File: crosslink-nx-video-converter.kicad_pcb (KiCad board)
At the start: 6 copper layers, 105.8 x 68 mm, 282 parts, among them J1 DC_SOCKET, J2 031-70526-21, J3 031-70526-21, J4 WE_68715014522_ONE-SIDE, J5 FTSH-105-01-F-DV-K, J6 WE_68715014522_ONE-SIDE, J7 2X05, J8 61300411121, Q1 2N7002, Q2 AO3401A, Q3 AO3401A, Q4 2N7002, Q5 AO3401A, Q6 2N7002, SW1 SW_DIP_x06, U1 MP20073, U10 AP7330-W5-7, U11 LIFCL-40-9BG256C, U12 MT41K128M16JT-125_K, U15 GS2971A, U16 GS2988, U17 SC18IS602BIPW, U18 W25Q32JVSSIQ, U2 LM339, U3 LM339, U5 AP62301WU-7, U6 AP62301WU-7, U7 AP62301WU-7, U8 AP7330-W5-7, U9 AP7330-W5-7, Y1 ABM7_27.000MH_D2Y_T, Y2 OSC40M-3.3_S5

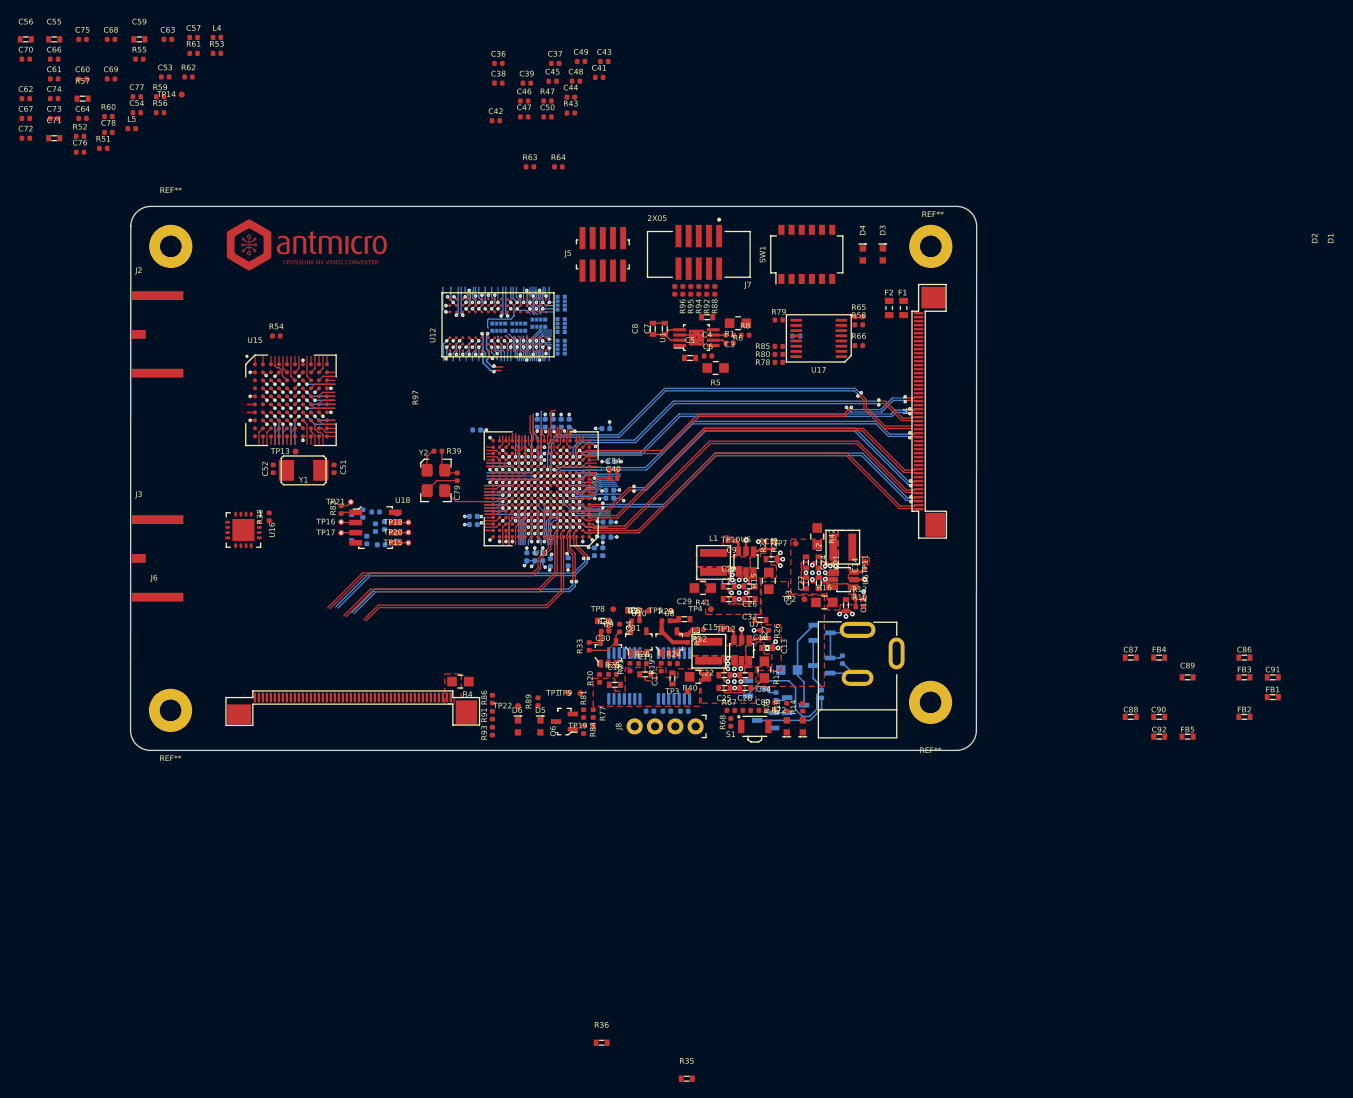
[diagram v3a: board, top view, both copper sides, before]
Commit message: Finished component placement
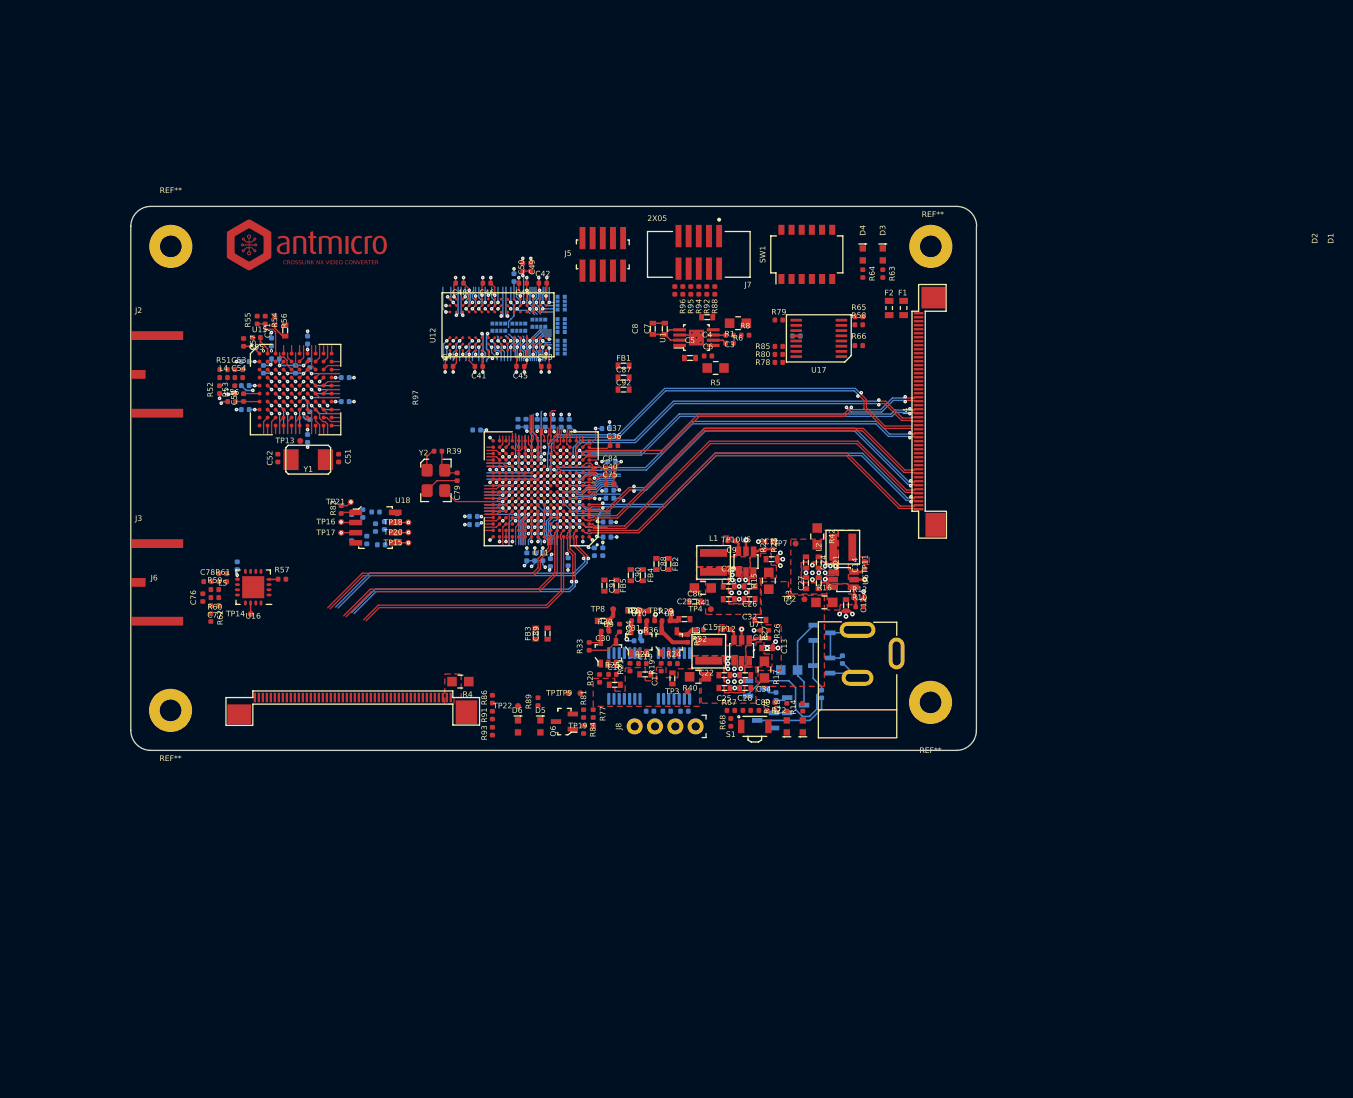
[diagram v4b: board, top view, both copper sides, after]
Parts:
- C38, C39, C60, C61, C62, C63, C64, C66, C67, C68, C69, C70, C72, C73, C74, R38, R47: moved to B.Cu
- C55: value C_47n_0603 -> C_47n_0402; footprint crosslink-nx-video-converter-footprints:0603-cap -> antmicro-footprints:0402-cap
- C56, C59: value C_470n_0603 -> C_470n_0402; footprint crosslink-nx-video-converter-footprints:0603-cap -> antmicro-footprints:0402-cap
- R35: value R_18k7_1%_0603 -> R_18k7_0402; footprint crosslink-nx-video-converter-footprints:0603-res -> antmicro-footprints:0402-res; moved to B.Cu
- R36: value R_15k_0603 -> R_15k_0402; footprint crosslink-nx-video-converter-footprints:0603-res -> antmicro-footprints:0402-res
- R43: value R_100R_0402 -> R_100R_0201; footprint crosslink-nx-video-converter-footprints:0402-res -> antmicro-footprints:0201-res; moved to B.Cu
- R57: value R_750R_0603 -> R_750R_0402; footprint crosslink-nx-video-converter-footprints:0603-res -> antmicro-footprints:0402-res
- moved FB1 91.1 mm to (136.6, 74.9)
- moved FB3 88.8 mm to (125.6, 108.4), turned to 90 degrees
- moved C75 86.2 mm to (134.9, 89.7)
- moved C91 84.3 mm to (134.2, 102.4), turned to -90 degrees
- moved C89 80.2 mm to (127.1, 108.4), turned to 90 degrees
- moved C92 79.8 mm to (136.6, 77.9)
- moved FB2 74.5 mm to (142.2, 99.7), turned to -90 degrees
- moved FB5 73.9 mm to (135.7, 102.4), turned to -90 degrees
- moved C87 72.4 mm to (136.6, 76.4)
- moved C86 69.1 mm to (145.5, 104.4)
- moved C90 68.4 mm to (137.5, 101.1), turned to -90 degrees
- moved R62 67.6 mm to (85.0, 106.4), turned to -90 degrees
- moved R61 66.1 mm to (86.5, 101.9)
- moved TP14 65.5 mm to (90.0, 106.0)
- moved FB4 65.4 mm to (139.0, 101.1), turned to -90 degrees
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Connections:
- C56 pad 1: Net-(C56-Pad1) -> GND
- C56 pad 2: GND -> Net-(U15-PadG1)
- C59 pad 1: Net-(C56-Pad1) -> Net-(U15-PadG1)
- U15 pad G1: Net-(C56-Pad1) -> Net-(U15-PadG1)
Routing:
- net GND: track 103.6 -> 144.0 mm, vias 158 -> 180
- net +1V5: track 17.5 -> 35.1 mm, vias 24 -> 32
- net +1V2: track 7.42 -> 16.7 mm, vias 9 -> 11
- net Vref: track 3.56 -> 12.0 mm, vias 3 -> 5
- net +3V3: track 14.9 -> 23.3 mm, vias 15 -> 17
- net Net-(R54-Pad2): track 1.00 -> 5.66 mm
- net Net-(U10-Pad4): track 0.00 -> 3.29 mm, vias 0 -> 1
- net Net-(U15-PadG1): track 0.00 -> 3.03 mm
- net /DDR3/DDR3_CKE: track 12.2 -> 9.33 mm
- net /DDR3/DDR3_LDQS_P: track 8.41 -> 5.62 mm, vias 3 -> 2
- net /DDR3/DDR3_ODT: track 8.61 -> 11.1 mm
- net /DDR3/DDR3_LDQS_N: track 8.83 -> 6.41 mm, vias 3 -> 2
- net Net-(R37-Pad1): track 1.33 -> 3.55 mm, vias 0 -> 1
- net Net-(C71-Pad1): track 1.00 -> 2.83 mm
- net Net-(TP14-Pad1): track 0.00 -> 1.38 mm
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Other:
- board size 105.8 x 68 mm -> 105.7 x 68 mm

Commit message: Loclib
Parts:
- C1, C100, C101, C102, C103, C104, C105, C106, C107, C14, C15, C16, C2, C3, C35, C36, C37, C38, C39, C40, C51, C52, C55, C56, C58, C59, C6, C60, C61, C62, C63, C64, C65, C66, C67, C68, C69, C70, C72, C73, C74, C75, C79, C80, C81, C82, C83, C84, C85, C9, C93, C94, C95, C96, C97, C98, C99: footprint antmicro-footprints:0402-cap -> crosslink-nx-video-converter-footprints:0402-cap
- C20, C21, C22, C23, C24, C25, C26, C27, C28, C32, C33, C34, C5, C7, C8: footprint antmicro-footprints:0603-cap -> crosslink-nx-video-converter-footprints:0603-cap
- J8: footprint antmicro-footprints:PinHeader_1x4_P2.54mm_Drill1.02mm -> crosslink-nx-video-converter-footprints:PinHeader_1x4_P2.54mm_Drill1.02mm
- R1, R10, R11, R12, R14, R18, R19, R2, R20, R21, R22, R23, R24, R25, R26, R27, R28, R29, R3, R30, R31, R32, R33, R34, R35, R36, R37, R38, R39, R54, R55, R57, R58, R63, R64, R65, R66, R67, R68, R69, R7, R70, R71, R72, R73, R74, R75, R76, R77, R78, R79, R8, R80, R81, R82, R83, R84, R85, R86, R87, R88, R89, R9, R90, R91, R92, R93, R94, R95, R96, R97: footprint antmicro-footprints:0402-res -> crosslink-nx-video-converter-footprints:0402-res
- R43: footprint antmicro-footprints:0201-res -> crosslink-nx-video-converter-footprints:0201-res
- TP1, TP10, TP11, TP12, TP13, TP14, TP15, TP16, TP17, TP18, TP19, TP2, TP20, TP21, TP22, TP3, TP4, TP5, TP6, TP7, TP8, TP9: footprint antmicro-footprints:Testpoint_smd_0_75mm -> crosslink-nx-video-converter-footprints:Testpoint_smd_0_75mm
- U1: footprint antmicro-footprints:MSOP-8-1EP_W3mm -> crosslink-nx-video-converter-footprints:MSOP-8-1EP_W3mm
- U11: footprint antmicro-footprints:BGA-256_16x16_14.0x14.0mm -> crosslink-nx-video-converter-footprints:BGA-256_16x16_14.0x14.0mm
- U2, U3: footprint antmicro-footprints:TSSOP-14_4.4x5mm_P0.65mm -> crosslink-nx-video-converter-footprints:TSSOP-14_4.4x5mm_P0.65mm

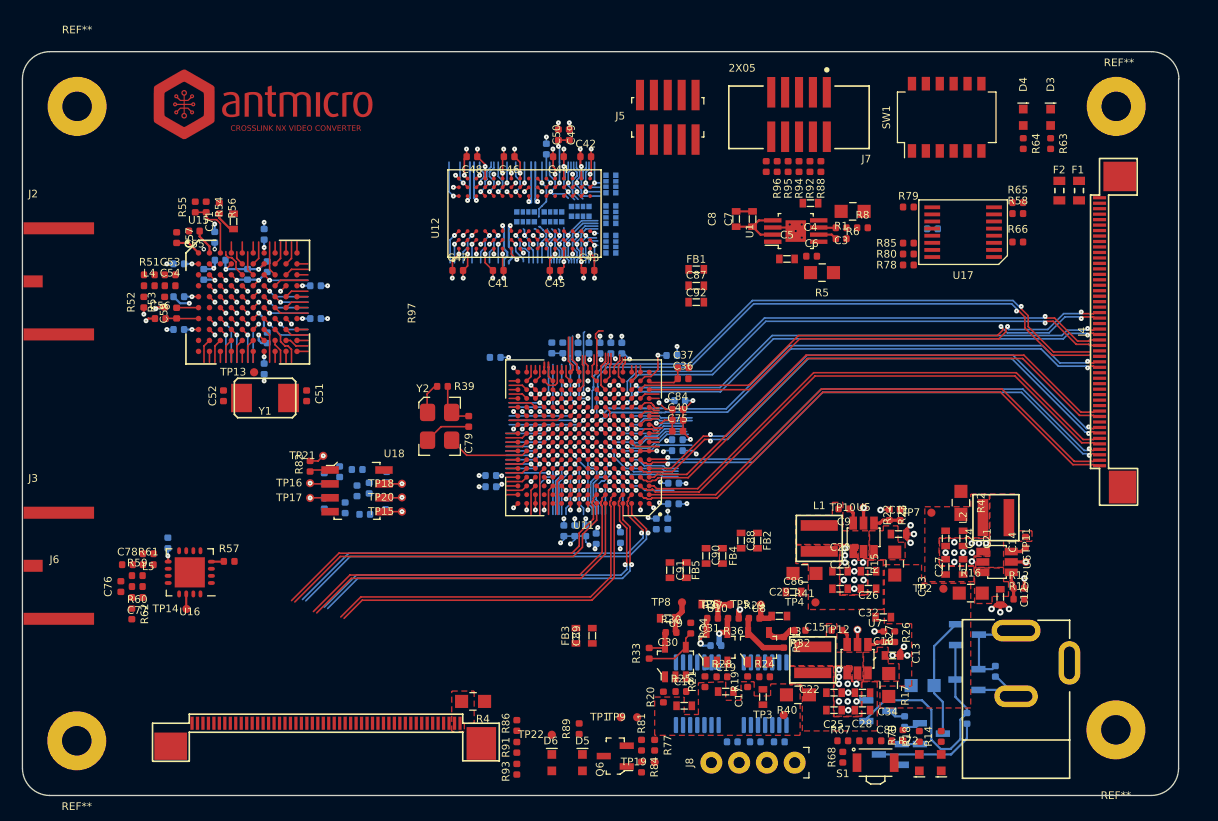
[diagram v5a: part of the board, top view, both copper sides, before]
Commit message: Routed DDR3 C&A
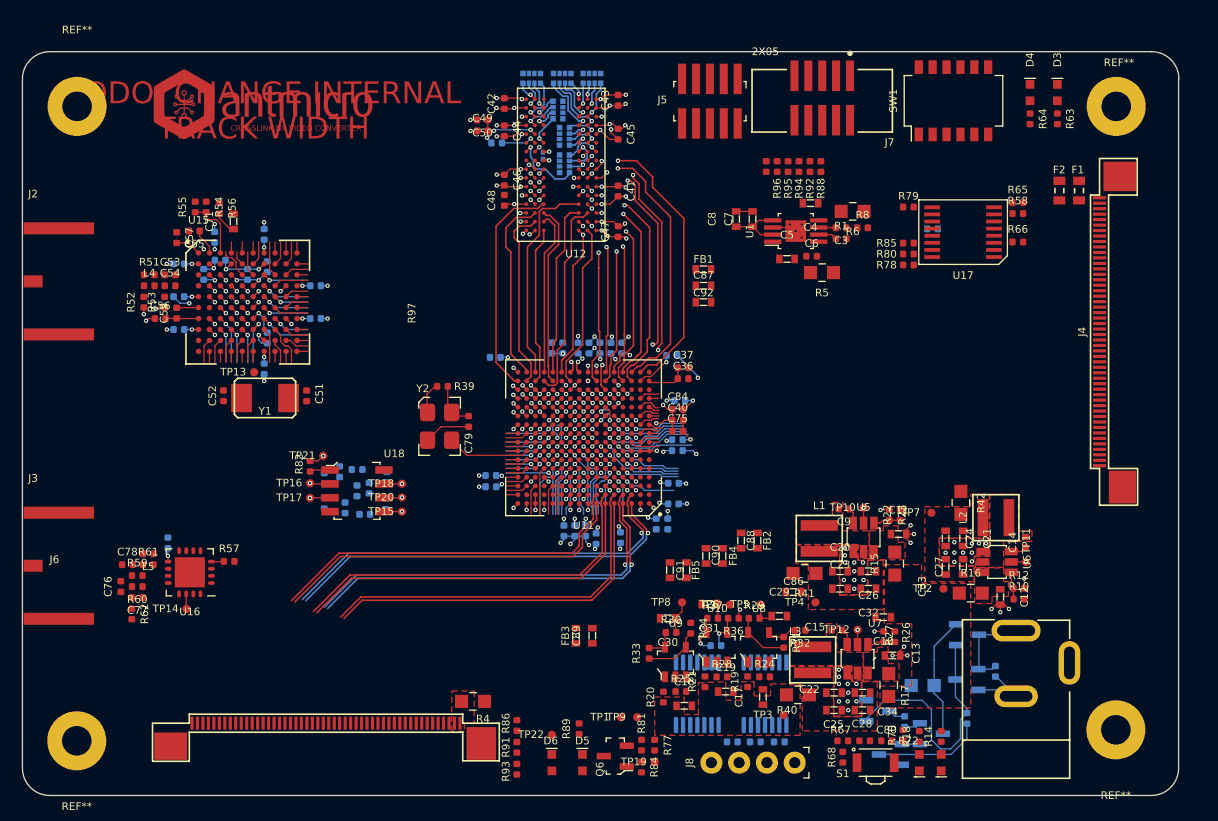
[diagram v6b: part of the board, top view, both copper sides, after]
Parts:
- moved C43 15.8 mm to (129.5, 59.4), turned to 90 degrees
- moved R45 15.3 mm to (127.1, 57.4), turned to 180 degrees
- moved C47 15.1 mm to (129.5, 71.4), turned to 90 degrees
- moved C45 13.7 mm to (129.5, 62.5), turned to -90 degrees
- moved R49 13.2 mm to (124.4, 57.4), turned to 180 degrees
- moved C41 13.1 mm to (129.5, 67.7), turned to -90 degrees
- moved R48 12.1 mm to (121.6, 57.4), turned to 180 degrees
- moved R46 9.49 mm to (124.0, 60.3), turned to 90 degrees
- moved C42 8.89 mm to (119.1, 59.7), turned to 90 degrees
- moved C50 8.06 mm to (117.1, 61.2), turned to 180 degrees
- moved R44 7.44 mm to (124.6, 62.7), turned to -90 degrees
- moved C49 6.95 mm to (117.1, 62.2), turned to 0 degrees
- moved R50 6.02 mm to (124.6, 65.2), turned to -90 degrees
- moved U12 5.58 mm to (124.3, 65.3), turned to 180 degrees
- moved C44 5.47 mm to (119.1, 62.2), turned to -90 degrees
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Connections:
- R44 pad 1: /DDR3/DDR3_A0 -> /DDR3/DDR3_BA0
- R44 pad 2: /DDR3/DDR3_A1 -> /DDR3/DDR3_BA2
- R44 pad 3: /DDR3/DDR3_A2 -> /DDR3/~{DDR3_CS}
- R44 pad 4: /DDR3/DDR3_A3 -> /DDR3/~{DDR3_WE}
- R45 pad 1: /DDR3/DDR3_A4 -> /DDR3/DDR3_A5
- R45 pad 2: /DDR3/DDR3_A5 -> /DDR3/DDR3_A7
- R45 pad 3: /DDR3/DDR3_A6 -> /DDR3/~{DDR3_RESET}
- R45 pad 4: /DDR3/DDR3_A7 -> /DDR3/DDR3_A9
- R46 pad 1: /DDR3/DDR3_A8 -> /DDR3/DDR3_A10
- R46 pad 2: /DDR3/DDR3_A9 -> /DDR3/DDR3_A12
- R46 pad 3: /DDR3/DDR3_A10 -> /DDR3/DDR3_BA1
- R46 pad 4: /DDR3/DDR3_A11 -> /DDR3/DDR3_A1
- R48 pad 1: /DDR3/DDR3_A12 -> /DDR3/DDR3_A4
- R48 pad 2: /DDR3/DDR3_A13 -> /DDR3/DDR3_A11
- R48 pad 3: /DDR3/DDR3_BA0 -> /DDR3/DDR3_A6
- R48 pad 4: /DDR3/DDR3_BA1 -> /DDR3/DDR3_A8
- R49 pad 1: /DDR3/~{DDR3_RESET} -> /DDR3/DDR3_A13
- R49 pad 2: /DDR3/~{DDR3_RAS} -> /DDR3/DDR3_A2
- R49 pad 3: /DDR3/~{DDR3_CAS} -> /DDR3/DDR3_A3
- R49 pad 4: /DDR3/~{DDR3_WE} -> /DDR3/DDR3_A0
- R50 pad 1: /DDR3/~{DDR3_CS} -> /DDR3/DDR3_ODT
- R50 pad 2: /DDR3/DDR3_ODT -> /DDR3/~{DDR3_CAS}
- R50 pad 3: /DDR3/DDR3_CKE -> /DDR3/~{DDR3_RAS}
- R50 pad 4: /DDR3/DDR3_BA2 -> /DDR3/DDR3_CKE
- U11 pad A11: unconnected-(U11-PadA11) -> (no net)
- U11 pad A12: unconnected-(U11-PadA12) -> (no net)
- U11 pad A14: GND -> (no net)
- U11 pad A15: GND -> (no net)
- U11 pad A3: /Peripherals/MIPI1_D2_P -> (no net)
- U11 pad A4: /Peripherals/MIPI1_D0_P -> (no net)
- U11 pad A5: /Peripherals/MIPI1_CLK_P -> (no net)
- U11 pad A6: /Peripherals/MIPI1_D1_P -> (no net)
- U11 pad A7: /Peripherals/MIPI1_D3_P -> (no net)
- U11 pad A9: GND -> (no net)
- U11 pad B1: /Peripherals/MIPI0_D3_P -> (no net)
- U11 pad B12: unconnected-(U11-PadB12) -> (no net)
- U11 pad B16: /FPGA/DONE -> (no net)
- U11 pad B2: /Peripherals/MIPI0_D3_N -> (no net)
- U11 pad B3: /Peripherals/MIPI1_D2_N -> (no net)
- U11 pad B4: /Peripherals/MIPI1_D0_N -> (no net)
- U11 pad B5: /Peripherals/MIPI1_CLK_N -> (no net)
- U11 pad B6: /Peripherals/MIPI1_D1_N -> (no net)
- U11 pad B7: /Peripherals/MIPI1_D3_N -> (no net)
- U11 pad B9: GND -> (no net)
- U11 pad C1: /Peripherals/MIPI0_D1_P -> (no net)
- U11 pad C11: GND -> (no net)
- U11 pad C12: /FPGA/PROGRAMN -> (no net)
- U11 pad C13: unconnected-(U11-PadC13) -> (no net)
- U11 pad C14: /FPGA/SPI_DQ0_MOSI -> (no net)
- U11 pad C15: /FPGA/~{FLASH_CS} -> (no net)
- U11 pad C16: /FPGA/SPI_CLK -> (no net)
- U11 pad C2: /Peripherals/MIPI0_D1_N -> (no net)
- U11 pad D1: /Peripherals/MIPI0_CLK_P -> (no net)
- U11 pad D10: JTAG_EN -> (no net)
- U11 pad D11: /FPGA/INITN -> (no net)
- U11 pad D12: /FPGA/SPI_DQ3 -> (no net)
- U11 pad D13: +3V3 -> (no net)
- U11 pad D15: /FPGA/SPI_DQ2 -> (no net)
- U11 pad D16: /FPGA/SPI_DQ1_MISO -> (no net)
- U11 pad D2: /Peripherals/MIPI0_CLK_N -> (no net)
- U11 pad D4: /SDI/RESET_TRST -> (no net)
- U11 pad D5: /SDI/STANDBY -> (no net)
- U11 pad D6: /SDI/SW_EN -> (no net)
- U11 pad E1: /Peripherals/MIPI0_D0_P -> (no net)
- U11 pad E10: /Peripherals/FFC2_VSYNC1 -> (no net)
- U11 pad E11: TMS -> (no net)
- U11 pad E12: unconnected-(U11-PadE12) -> (no net)
- U11 pad E13: /Peripherals/FCC2_SDA2 -> (no net)
- U11 pad E14: TDO -> (no net)
- U11 pad E15: LED0 -> (no net)
- U11 pad E16: LED1 -> (no net)
- U11 pad E2: /Peripherals/MIPI0_D0_N -> (no net)
- U11 pad E4: /SDI/~{CS_TMS} -> (no net)
- U11 pad E5: /SDI/SCLK_TCK -> (no net)
- U11 pad E6: /SDI/TIM_861 -> (no net)
- U11 pad E9: /Peripherals/FFC2_RESET -> (no net)
- U11 pad F1: /Peripherals/MIPI0_D2_P -> (no net)
- U11 pad F10: /Peripherals/FFC1_RESET -> (no net)
- U11 pad F11: TDI -> (no net)
- U11 pad F13: +3V3 -> (no net)
- U11 pad F14: TCK -> (no net)
- U11 pad F15: /Peripherals/FCC2_SCL2 -> (no net)
- U11 pad F16: /Peripherals/FFC1_VSYNC0 -> (no net)
- U11 pad F2: /Peripherals/MIPI0_D2_N -> (no net)
- U11 pad F4: /SDI/SDOUT_TDO -> (no net)
- U11 pad F5: +3V3 -> (no net)
- U11 pad F6: /SDI/SDIN_TDI -> (no net)
- U11 pad F9: /Peripherals/FFC2_VSYNC0 -> (no net)
- U11 pad G10: SCL -> (no net)
- U11 pad G11: /Peripherals/FCC1_SDA1 -> (no net)
- U11 pad G12: /Peripherals/FCC1_SCL1 -> (no net)
- U11 pad G13: /Peripherals/FCC1_SDA2 -> (no net)
- U11 pad G14: /Peripherals/FCC1_SCL2 -> (no net)
- U11 pad G15: 40MHz_3V3 -> (no net)
- U11 pad G16: /Peripherals/FFC1_VSYNC1 -> (no net)
- U11 pad G3: /SDI/SDI_STAT5 -> (no net)
- U11 pad G4: /SDI/~{SDO_DISABLE} -> (no net)
- U11 pad G6: /SDI/SDO_EN/DIS -> (no net)
- U11 pad G9: SDA -> (no net)
- U11 pad H1: /SDI/SDI_D4 -> (no net)
- U11 pad H2: /SDI/SDI_D5 -> (no net)
- U11 pad H3: /SDI/SDI_D3 -> (no net)
- U11 pad H4: /SDI/SDI_D2 -> (no net)
- U11 pad H5: /SDI/SDI_D1 -> (no net)
- U11 pad H6: /SDI/SDI_D0 -> (no net)
- U11 pad J1: /SDI/SDI_D7 -> (no net)
- U11 pad J2: /SDI/SDI_D8 -> (no net)
- U11 pad J4: +3V3 -> (no net)
- U11 pad J5: /SDI/SDI_D6 -> (no net)
- U11 pad J6: /SDI/SDI_PCLK -> (no net)
- U11 pad K1: /SDI/SDI_D9 -> (no net)
- U11 pad K2: /SDI/SDI_D10 -> (no net)
- U11 pad K3: /SDI/SDI_D12 -> (no net)
- U11 pad K4: /SDI/SDI_D11 -> (no net)
- U11 pad K5: /SDI/SDI_D14 -> (no net)
- U11 pad K6: /SDI/SDI_D13 -> (no net)
- U11 pad L1: /SDI/SDI_D15 -> (no net)
- U11 pad L10: /DDR3/DDR3_A8 -> /DDR3/DDR3_A7
- U11 pad L11: /DDR3/DDR3_A7 -> /DDR3/DDR3_A13
- U11 pad L12: /DDR3/DDR3_A10 -> /DDR3/DDR3_A8
- U11 pad L2: /SDI/SDI_D16 -> (no net)
- U11 pad L3: /SDI/SDI_STAT2 -> (no net)
- U11 pad L4: /SDI/SDI_D19 -> (no net)
- U11 pad L5: /SDI/SDI_STAT0 -> (no net)
- U11 pad L8: /DDR3/DDR3_BA2 -> /DDR3/DDR3_A9
- U11 pad L9: /DDR3/~{DDR3_RAS} -> /DDR3/~{DDR3_RESET}
- U11 pad M1: /SDI/SDI_D17 -> (no net)
- U11 pad M10: /DDR3/DDR3_ODT -> /DDR3/DDR3_BA2
- U11 pad M12: /DDR3/DDR3_A6 -> /DDR3/~{DDR3_RAS}
- U11 pad M13: /DDR3/DDR3_A9 -> /DDR3/DDR3_A6
- U11 pad M14: /DDR3/DDR3_A3 -> /DDR3/DDR3_A11
- U11 pad M16: /DDR3/DDR3_A11 -> /DDR3/DDR3_A4
- U11 pad M2: /SDI/SDI_D18 -> (no net)
- U11 pad M3: /SDI/SDI_STAT1 -> (no net)
- U11 pad N1: /SDI/SDI_STAT4 -> (no net)
- U11 pad N10: /DDR3/~{DDR3_RESET} -> /DDR3/~{DDR3_CS}
- U11 pad N13: /DDR3/DDR3_A0 -> /DDR3/DDR3_CKE
- U11 pad N15: /DDR3/DDR3_A5 -> /DDR3/DDR3_A12
- U11 pad N16: /DDR3/DDR3_A4 -> /DDR3/DDR3_A1
- U11 pad N2: /SDI/SDI_STAT3 -> (no net)
- U11 pad N8: /DDR3/~{DDR3_CAS} -> /DDR3/DDR3_A2
- U11 pad N9: /DDR3/~{DDR3_WE} -> /DDR3/DDR3_A5
- U11 pad P15: /DDR3/DDR3_A1 -> /DDR3/DDR3_A10
- U11 pad P16: /DDR3/DDR3_A2 -> /DDR3/DDR3_BA1
- U11 pad P6: /DDR3/DDR3_BA0 -> /DDR3/~{DDR3_WE}
- U11 pad P7: /DDR3/DDR3_BA1 -> /DDR3/DDR3_A3
- U11 pad P8: /DDR3/~{DDR3_CS} -> /DDR3/DDR3_A0
- U11 pad P9: /DDR3/DDR3_CKE -> /DDR3/DDR3_BA0
- U11 pad R10: /DDR3/DDR3_DQ8 -> /DDR3/DDR3_DQ13
- U11 pad R15: /DDR3/DDR3_UDM -> /DDR3/DDR3_DQ14
- U11 pad R16: /DDR3/DDR3_DQ15 -> /DDR3/DDR3_DQ8
- U11 pad R3: /DDR3/DDR3_DQ0 -> /DDR3/DDR3_DQ2
- U11 pad R4: /DDR3/DDR3_DQ3 -> /DDR3/DDR3_DQ5
- U11 pad R6: /DDR3/DDR3_DQ5 -> /DDR3/DDR3_DQ3
- U11 pad R7: /DDR3/DDR3_DQ7 -> /DDR3/DDR3_LDM
- U11 pad T11: /DDR3/DDR3_DQ10 -> /DDR3/DDR3_DQ15
- U11 pad T14: /DDR3/DDR3_DQ13 -> /DDR3/DDR3_UDM
- U11 pad T15: /DDR3/DDR3_DQ14 -> /DDR3/DDR3_DQ10
- U11 pad T2: /DDR3/DDR3_LDM -> /DDR3/DDR3_DQ4
- U11 pad T3: /DDR3/DDR3_DQ1 -> /DDR3/DDR3_DQ6
- U11 pad T4: /DDR3/DDR3_DQ2 -> /DDR3/DDR3_DQ0
- U11 pad T5: /DDR3/DDR3_DQ4 -> /DDR3/DDR3_DQ7
- U11 pad T6: /DDR3/DDR3_DQ6 -> /DDR3/DDR3_DQ1
- U11 pad T7: /DDR3/DDR3_A12 -> /DDR3/DDR3_ODT
- U11 pad T8: /DDR3/DDR3_A13 -> /DDR3/~{DDR3_CAS}
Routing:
- net /DDR3/DDR3_A13: track 2.35 -> 65.2 mm, vias 1 -> 2
- net /Peripherals/MIPI2_D2_P: track 55.2 -> 0.57 mm, vias 2 -> 1
- net /Peripherals/MIPI2_D2_N: track 54.7 -> 0.57 mm, vias 2 -> 1
- net /DDR3/~{DDR3_RESET}: track 6.77 -> 58.4 mm
- net /Peripherals/MIPI0_D0_N: track 49.5 -> 0.00 mm, vias 2 -> 0
- net /Peripherals/MIPI0_D1_N: track 49.2 -> 0.00 mm
- net /Peripherals/MIPI0_CLK_N: track 49.0 -> 0.00 mm
- net /Peripherals/MIPI0_D3_N: track 49.0 -> 0.00 mm
- net /Peripherals/MIPI2_D1_N: track 48.8 -> 0.00 mm, vias 2 -> 0
- net /Peripherals/MIPI0_D0_P: track 48.5 -> 0.00 mm, vias 2 -> 0
- net /Peripherals/MIPI2_D1_P: track 48.3 -> 0.00 mm, vias 2 -> 0
- net /Peripherals/MIPI2_D3_P: track 49.7 -> 1.39 mm, vias 2 -> 1
- net /Peripherals/MIPI0_D1_P: track 48.2 -> 0.00 mm
- net /Peripherals/MIPI2_D3_N: track 49.7 -> 1.56 mm, vias 2 -> 1
- net /Peripherals/MIPI0_CLK_P: track 48.0 -> 0.00 mm
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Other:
- board text added: "TODO: CHANGE INTERNAL TRACK WIDTH"
